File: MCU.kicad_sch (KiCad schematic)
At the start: 1 part, among them U201 ESP32-C3-MINI-1-N4

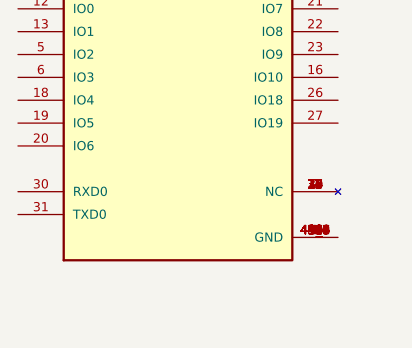
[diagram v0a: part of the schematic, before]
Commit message: finished ADC side, may add some additional bare channels, started DAC part and need to add the tca0372 amplifier or think about it
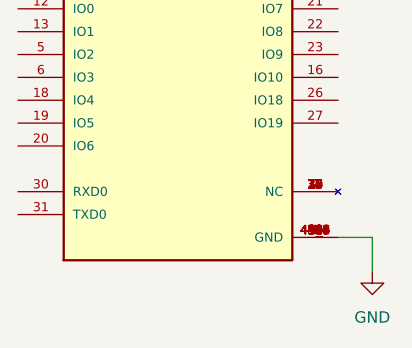
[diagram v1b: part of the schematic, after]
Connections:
- net GND: now reaches U201.1 (GND), U201.11 (GND), U201.14 (GND), U201.2 (GND), U201.36 (GND), U201.37 (GND), U201.38 (GND), U201.39 (GND), U201.40 (GND), U201.41 (GND), U201.42 (GND), U201.43 (GND), U201.44 (GND), U201.45 (GND), U201.46 (GND), U201.47 (GND), U201.48 (GND), U201.49_1 (GND), U201.49_2 (GND), U201.49_3 (GND), U201.49_4 (GND), U201.49_5 (GND), U201.49_6 (GND), U201.49_7 (GND), U201.49_8 (GND), U201.49_9 (GND), U201.50 (GND), U201.51 (GND), U201.52 (GND), U201.53 (GND)
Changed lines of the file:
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@@
 		(company "Elnady Electronics")
+	)
+	(wire
+		(pts
+			(xy 154.94 106.68) (xy 154.94 110.49)
+		)
+		(stroke
+			(width 0)
+			(type default)
+		)
+	)
+	(wire
+		(pts
+			(xy 151.13 106.68) (xy 154.94 106.68)
+		)
+		(stroke
+			(width 0)
+			(type default)
+		)
 	)
 	(symbol
@@
 					(unit 1)
 				)
+			)
+		)
+	)
+	(symbol
+		(lib_id "power:GND")
+		(at 154.94 110.49 0)
+		(unit 1)
+		(exclude_from_sim no)
+		(in_bom yes)
+		(on_board yes)
+		(dnp no)
+		(fields_autoplaced yes)
+		(property "Reference" "#PWR0201"
+			(at 154.94 116.84 0)
+			(effects
+				(font
+					(size 1.27 1.27)
+				)
+				(hide yes)
+			)
+		)
+		(property "Value" "GND"
+			(at 154.94 115.57 0)
+			(effects
+				(font
+					(size 1.27 1.27)
+				)
+			)
+		)
+		(property "Footprint" ""
+			(at 154.94 110.49 0)
+			(effects
+				(font
+					(size 1.27 1.27)
+				)
+				(hide yes)
+			)
+		)
+		(property "Datasheet" ""
+			(at 154.94 110.49 0)
+			(effects
+				(font
+					(size 1.27 1.27)
+				)
+				(hide yes)
+			)
+		)
+		(property "Description" "Power symbol creates a global label with name \"GND\" , ground"
+			(at 154.94 110.49 0)
+			(effects
+				(font
+					(size 1.27 1.27)
+				)
+				(hide yes)
+			)
+		)
+		(pin "1"
+		)
+		(instances
+			(project "NadyScope"
+				(path "/eb93e2be-0074-48a1-b88c-5129bddcbd28/f0b6941f-10e7-4982-bf52-9e94023a051f"
+					(reference "#PWR0201")
+					(unit 1)
+				)

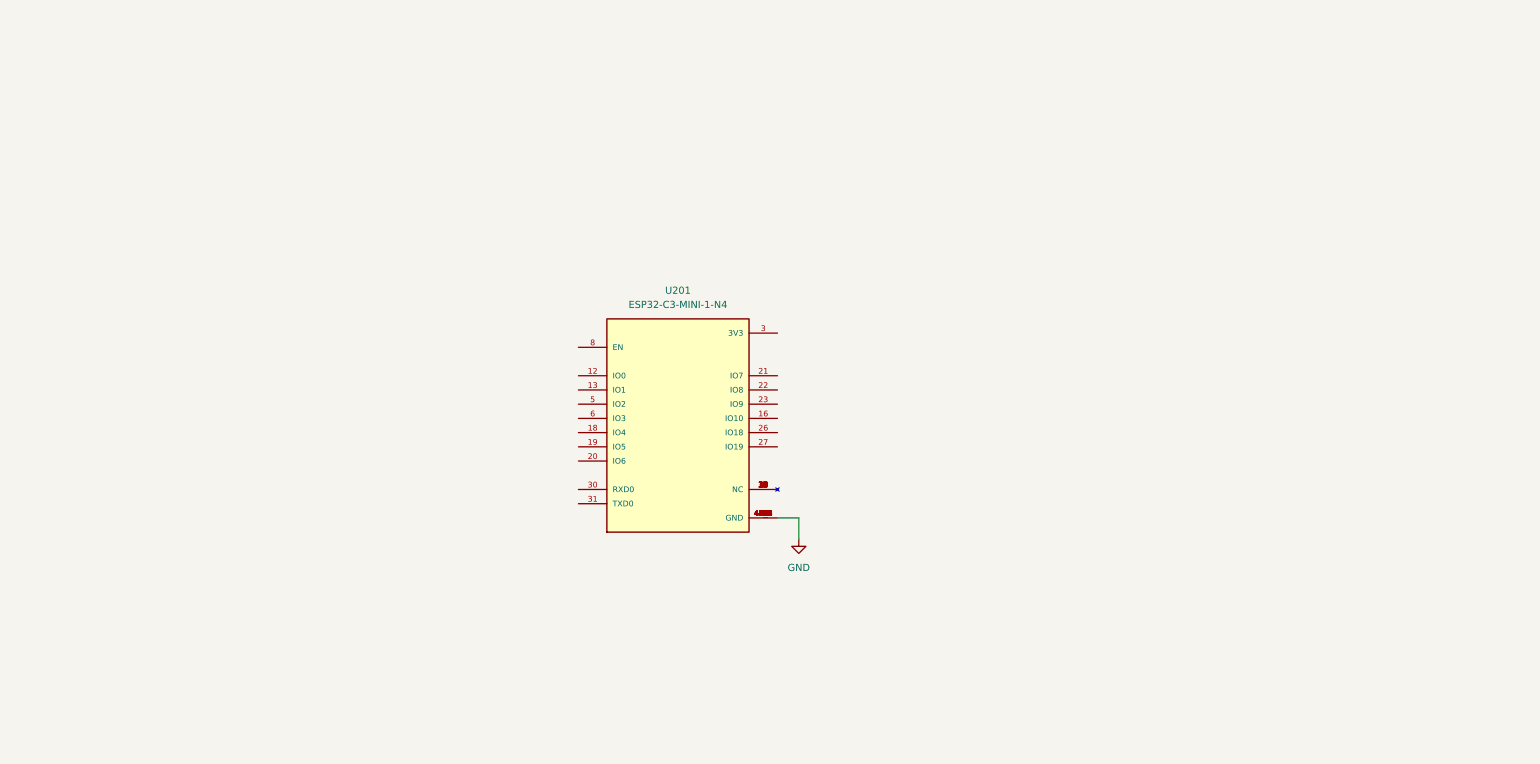
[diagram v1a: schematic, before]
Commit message: 80% done, maybe add more AINs, finish the power circuit and add system & block diagrams
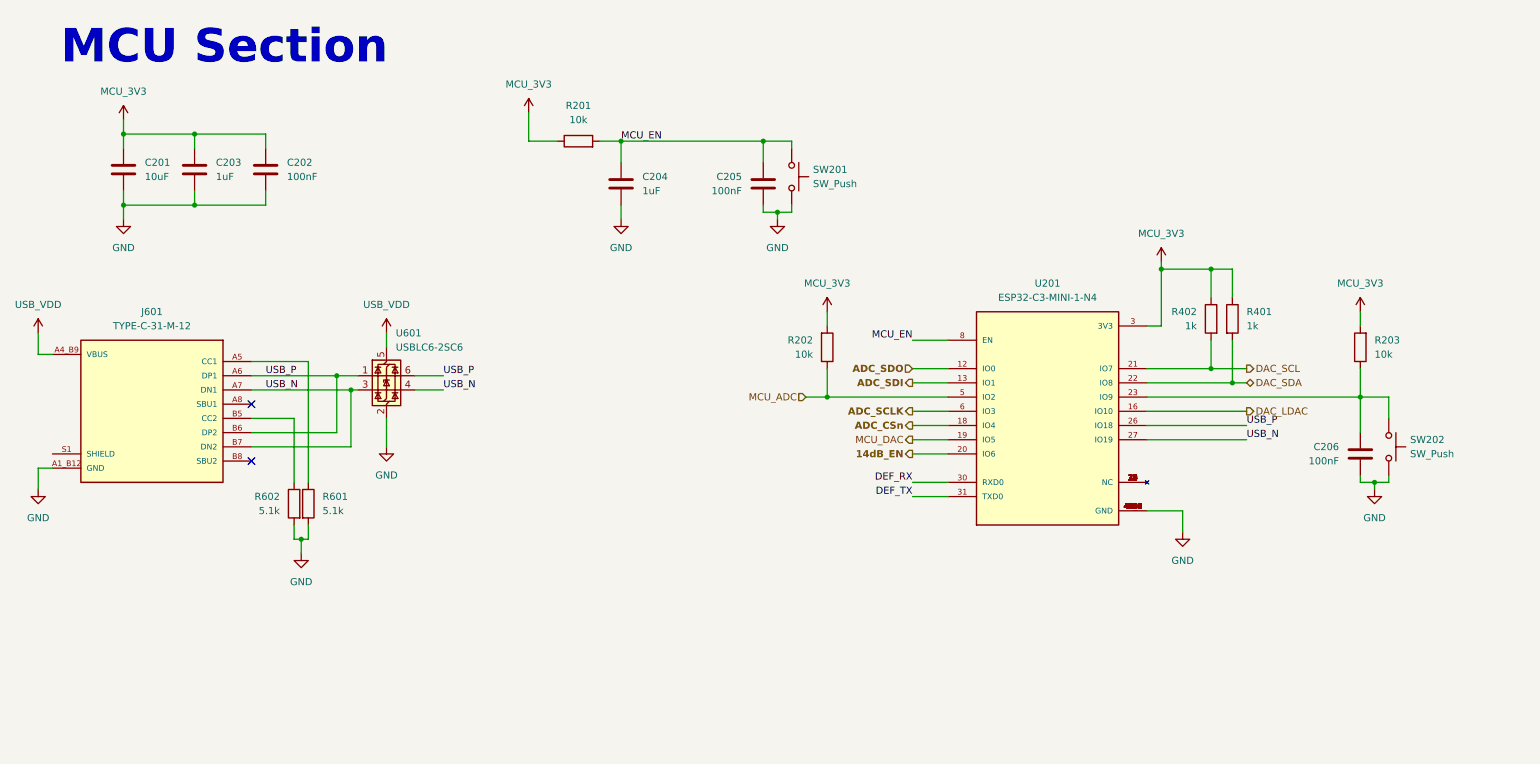
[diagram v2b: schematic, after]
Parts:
- added C201: 10uF, symbol Device:C
- added C202, C205, C206: 100nF, symbol Device:C
- added C203, C204: 1uF, symbol Device:C
- added J601: TYPE-C-31-M-12, TYPE-C-31-M-12:HRO_TYPE-C-31-M-12, symbol TYPE-C-31-M-12:TYPE-C-31-M-12
- added R201, R202, R203: 10k, symbol Device:R
- added R401, R402: 1k, symbol Device:R
- added R601, R602: 5.1k, symbol Device:R
- added SW201, SW202: SW_Push, symbol Switch:SW_Push
- added U601: USBLC6-2SC6, Package_TO_SOT_SMD:SOT-23-6, symbol Power_Protection:USBLC6-2SC6
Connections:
- net GND: now also C201.2, C202.2, C203.2, C204.2, C205.2, C206.2, J601.A1_B12 (GND), J601.B1_A12 (GND), R601.2, R602.2, SW201.2, SW202.2, U601.2 (GND)
- net ADC_SDO: now reaches U201.12 (IO0)
- net ADC_SDI: now reaches U201.13 (IO1)
- net DAC_LDAC: now reaches U201.16 (IO10)
- net ADC_CSn: now reaches U201.18 (IO4)
- net MCU_DAC: now reaches U201.19 (IO5)
- net 14dB_EN: now reaches U201.20 (IO6)
- net DAC_SCL: now reaches U201.21 (IO7)
- net DAC_SCL: now also R402.2
- net DAC_SDA: now reaches U201.22 (IO8)
- net DAC_SDA: now also R401.2
- net at U201.23 (IO9): now also C206.1, R203.1, SW202.1
- net USB_P: now reaches U201.26 (IO18)
- net USB_P: now also J601.A6 (DP1), J601.B6 (DP2), U601.1 (I/O1), U601.6 (I/O1)
- net USB_N: now reaches U201.27 (IO19)
- net USB_N: now also J601.A7 (DN1), J601.B7 (DN2), U601.3 (I/O2), U601.4 (I/O2)
- net MCU_3V3: now reaches U201.3 (3V3)
- net MCU_3V3: now also C201.1, C202.1, C203.1, R201.1, R202.2, R203.2, R401.1, R402.1
- net DEF_RX: now reaches U201.30 (RXD0)
- net DEF_TX: now reaches U201.31 (TXD0)
- net MCU_ADC: now reaches U201.5 (IO2)
- net MCU_ADC: now also R202.1
- net ADC_SCLK: now reaches U201.6 (IO3)
- net MCU_EN: now reaches U201.8 (EN)
- net MCU_EN: now also C204.1, C205.1, R201.2, SW201.1
- new net: J601.A5 (CC1), R601.1
- new net: J601.B5 (CC2), R602.1
- new net: J601.S1 (SHIELD), J601.S2 (SHIELD), J601.S3 (SHIELD), J601.S4 (SHIELD)
- new net USB_VDD: J601.A4_B9 (VBUS), J601.B4_A9 (VBUS), U601.5 (VBUS)
- no-connect marks 0 -> 2
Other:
- note added: "MCU Section"
- moved on the sheet: U201

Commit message: finished individual block placement and started integrating, might need to change the AFEs length
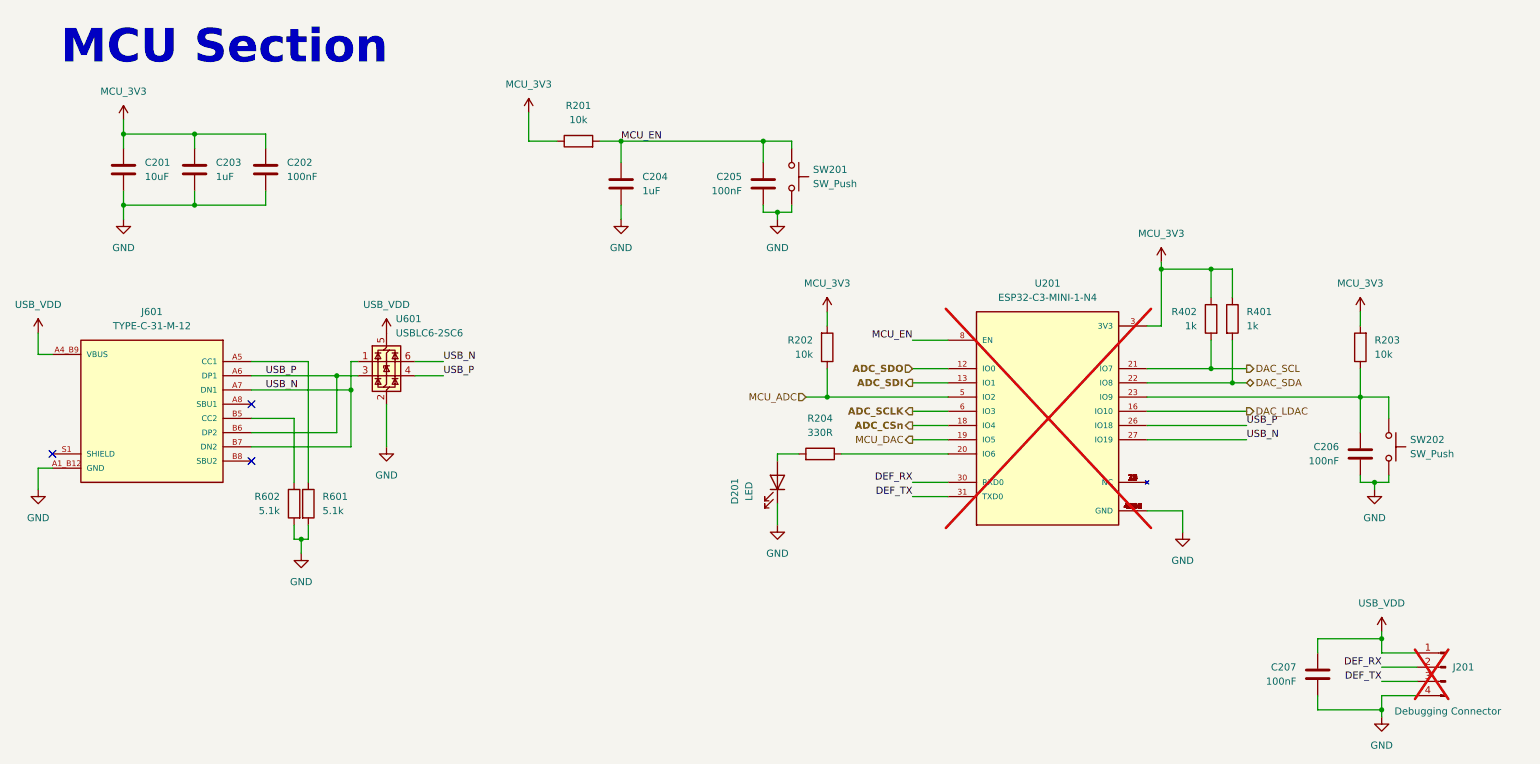
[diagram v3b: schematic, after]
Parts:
- added C207: 100nF, Capacitor_SMD:C_0603_1608Metric, symbol Device:C
- added D201: LED, LED_SMD:LED_0805_2012Metric, symbol Device:LED
- added J201: Debugging Connector, Connector_PinHeader_2.54mm:PinHeader_1x04_P2.54mm_Vertical, symbol Connector:Conn_01x04_Pin
- added R204: 330R, Resistor_SMD:R_0603_1608Metric, symbol Device:R
- C201: footprint (none) -> Capacitor_SMD:C_0603_1608Metric; MPN (none) -> CL10A106MP8NNNC
- C202, C205, C206: footprint (none) -> Capacitor_SMD:C_0603_1608Metric; MPN (none) -> 0603B104M250CT
- C203, C204: footprint (none) -> Capacitor_SMD:C_0603_1608Metric; MPN (none) -> 0603X105K250CT
- J601: MPN (none) -> TYPE-C-31-M-12
- R201, R202, R203: footprint (none) -> Resistor_SMD:R_0603_1608Metric; MPN (none) -> TD03G1002BT
- R401, R402: footprint (none) -> Resistor_SMD:R_0603_1608Metric; MPN (none) -> RT0603BRD071KL
- R601, R602: footprint (none) -> Resistor_SMD:R_0603_1608Metric; MPN (none) -> RT0603BRD075K1L
- SW201, SW202: footprint (none) -> Button_Switch_SMD:SW_Push_SPST_NO_Alps_SKRK
- U201: MPN (none) -> ESP32-C3-MINI-1-N4; now not fitted
- U601: MPN (none) -> USBLC6-2SC6
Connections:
- net DEF_RX: now also J201.2 (Pin_2)
- net DEF_TX: now also J201.3 (Pin_3)
- net GND: now also C207.2, D201.1 (K), J201.4 (Pin_4)
- net USB_N: now also U601.1 (I/O1), U601.6 (I/O1); no longer U601.3 (I/O2), U601.4 (I/O2)
- net USB_P: now also U601.3 (I/O2), U601.4 (I/O2); no longer U601.1 (I/O1), U601.6 (I/O1)
- net USB_VDD: now also C207.1, J201.1 (Pin_1)
- net 14dB_EN: no longer names the net of U201.20 (IO6)
- net 14dB_EN: now also R204.1
- new net: D201.2 (A), R204.2
- no-connect marks 2 -> 3
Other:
- moved on the sheet: U601

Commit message: DONE, ready for ordering
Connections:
- net ADC_SCLK: now also U201.13 (IO1); no longer U201.6 (IO3)
- net ADC_SDI: now also U201.6 (IO3); no longer U201.13 (IO1)
- net ADC_SDO: now also U201.16 (IO10); no longer U201.12 (IO0)
- net DAC_LDAC: now also U201.20 (IO6); no longer U201.16 (IO10)
- net DAC_SCL: now also R401.2, U201.22 (IO8); no longer R402.2, U201.21 (IO7)
- net DAC_SDA: now also R402.2, U201.21 (IO7); no longer R401.2, U201.22 (IO8)
- net MCU_ADC: now also U201.12 (IO0); no longer R202.1, U201.5 (IO2)
- net USB_N: now also U201.26 (IO18), U601.3 (I/O2), U601.4 (I/O2); no longer U201.27 (IO19), U601.1 (I/O1), U601.6 (I/O1)
- net USB_P: now also U201.27 (IO19), U601.1 (I/O1), U601.6 (I/O1); no longer U201.26 (IO18), U601.3 (I/O2), U601.4 (I/O2)
- net MCU_LED: now reaches R204.1
- net MCU_LED: now also R202.1, U201.5 (IO2); no longer U201.20 (IO6)
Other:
- moved on the sheet: D201, R204, U601
